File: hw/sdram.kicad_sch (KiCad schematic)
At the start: 25 parts, among them U1 NDS36PT5-16ET, U8 T20Q144xx, X2 ECS-2520MV-250-CM

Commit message: cleanup of trion project
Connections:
- net A11 renamed SDRAM_A11
- net A12 renamed SDRAM_A12
- net CKE renamed SDRAM_CKE
- net ETH0_CLK_OUT: no longer names the net of U8.93 (GPIOR_123_CLK12_CDI20)
- net ETH0_GPIO_1: no longer names the net of U8.89 (GPIOR_129_CTRL10)
- net ETH0_GPIO_2: no longer names the net of U8.90 (GPIOR_128_CTRL11)
- net LED0: no longer names the net of U8.92 (GPIOR_125_CLK10)
- net LED1: no longer names the net of U8.84 (GPIOR_135_CDI17)
- net LED2: no longer names the net of U8.83 (GPIOR_136_CDI16)
- net LED3: no longer names the net of U8.82 (GPIOR_138)
- net LED4: no longer names the net of R22.2, U8.80 (GPIOR_149_CBUS2)
- net LED5: no longer names the net of R23.2, U8.79 (GPIOR_150_CBUS1)
- net LED6: no longer names the net of R24.2, U8.78 (GPIOR_151_CBUS0)
- net LED7: no longer names the net of U8.76 (GPIOR_155)
- no-connect marks 2 -> 13
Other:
- moved on the sheet: R1
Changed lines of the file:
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@@
   (junction (at 67.31 45.72) (diameter 0) (color 0 0 0 0)
   )
+  (junction (at 24.638 101.6) (diameter 0) (color 0 0 0 0)
+  )
   (junction (at 45.72 166.37) (diameter 0) (color 0 0 0 0)
   )
   (junction (at 48.26 40.64) (diameter 0) (color 0 0 0 0)
   )
-  (junction (at 31.75 101.6) (diameter 0) (color 0 0 0 0)
-  )
   (junction (at 38.1 168.91) (diameter 0) (color 0 0 0 0)
   )
@@
   (junction (at 74.93 40.64) (diameter 0) (color 0 0 0 0)
   )
+  (no_connect (at 27.94 171.45))
+  (no_connect (at 160.02 151.13))
+  (no_connect (at 215.9 151.13))
+  (no_connect (at 148.59 97.79))
+  (no_connect (at 116.84 166.37))
+  (no_connect (at 160.02 148.59))
   (no_connect (at 219.71 113.03))
+  (no_connect (at 160.02 146.05))
+  (no_connect (at 215.9 148.59))
+  (no_connect (at 27.94 168.91))
+  (no_connect (at 215.9 146.05))
   (no_connect (at 219.71 110.49))
+  (no_connect (at 27.94 166.37))
   (wire (pts (xy 107.95 168.91) (xy 128.27 168.91))
     (stroke (width 0) (type default))
@@
     (stroke (width 0) (type default))
   )
+  (wire (pts (xy 24.638 101.6) (xy 44.45 101.6))
+    (stroke (width 0) (type default))
+  )
   (wire (pts (xy 57.15 124.46) (xy 57.15 125.73))
     (stroke (width 0) (type default))
@@
     (stroke (width 0) (type default))
   )
-  (wire (pts (xy 31.75 101.6) (xy 44.45 101.6))
-    (stroke (width 0) (type default))
-  )
   (wire (pts (xy 71.12 45.72) (xy 74.93 45.72))
     (stroke (width 0) (type default))
@@
     (stroke (width 0) (type default))
   )
-  (wire (pts (xy 31.75 100.33) (xy 31.75 101.6))
+  (wire (pts (xy 24.638 100.33) (xy 24.638 101.6))
     (stroke (width 0) (type default))
   )
@@
     (stroke (width 0) (type default))
   )
-  (wire (pts (xy 27.94 101.6) (xy 31.75 101.6))
+  (wire (pts (xy 20.828 101.6) (xy 24.638 101.6))
     (stroke (width 0) (type default))
   )
@@
     (effects (font (size 1.27 1.27)) (justify left bottom))
   )
-  (label "CSb" (at 27.94 101.6 180) (fields_autoplaced)
+  (label "CSb" (at 20.828 101.6 180) (fields_autoplaced)
     (effects (font (size 1.27 1.27)) (justify right bottom))
   )
@@
     )
   )
-  (global_label "LED0" (shape output) (at 160.02 146.05 180) (fields_autoplaced)
-    (effects (font (size 1.27 1.27)) (justify right))
-    (property "Intersheetrefs" "${INTERSHEET_REFS}" (at 152.3782 146.05 0)
-      (effects (font (size 1.27 1.27)) (justify right) hide)
-    )
-  )
-  (global_label "LED6" (shape output) (at 27.94 171.45 180) (fields_autoplaced)
-    (effects (font (size 1.27 1.27)) (justify right))
-    (property "Intersheetrefs" "${INTERSHEET_REFS}" (at 20.2982 171.45 0)
-      (effects (font (size 1.27 1.27)) (justify right) hide)
-    )
-  )
   (global_label "ULPI_NXT" (shape input) (at 219.71 123.19 0) (fields_autoplaced)
     (effects (font (size 1.27 1.27)) (justify left))
@@
     )
   )
-  (global_label "ETH0_GPIO_2" (shape bidirectional) (at 160.02 148.59 180) (fields_autoplaced)
-    (effects (font (size 1.27 1.27)) (justify right))
-    (property "Intersheetrefs" "${INTERSHEET_REFS}" (at 143.6469 148.59 0)
-      (effects (font (size 1.27 1.27)) (justify right) hide)
-    )
-  )
-  (global_label "ETH0_CLK_OUT" (shape bidirectional) (at 148.59 97.79 0) (fields_autoplaced)
-    (effects (font (size 1.27 1.27)) (justify left))
-    (property "Intersheetrefs" "${INTERSHEET_REFS}" (at 166.475 97.79 0)
-      (effects (font (size 1.27 1.27)) (justify left) hide)
-    )
-  )
-  (global_label "LED7" (shape output) (at 116.84 166.37 0) (fields_autoplaced)
-    (effects (font (size 1.27 1.27)) (justify left))
-    (property "Intersheetrefs" "${INTERSHEET_REFS}" (at 124.4818 166.37 0)
-      (effects (font (size 1.27 1.27)) (justify left) hide)
-    )
-  )
-  (global_label "LED3" (shape output) (at 215.9 151.13 0) (fields_autoplaced)
-    (effects (font (size 1.27 1.27)) (justify left))
-    (property "Intersheetrefs" "${INTERSHEET_REFS}" (at 223.5418 151.13 0)
-      (effects (font (size 1.27 1.27)) (justify left) hide)
-    )
-  )
-  (global_label "LED5" (shape output) (at 27.94 168.91 180) (fields_autoplaced)
-    (effects (font (size 1.27 1.27)) (justify right))
-    (property "Intersheetrefs" "${INTERSHEET_REFS}" (at 20.2982 168.91 0)
-      (effects (font (size 1.27 1.27)) (justify right) hide)
-    )
-  )
   (global_label "SDRAM_A5" (shape input) (at 44.45 78.74 180) (fields_autoplaced)
     (effects (font (size 1.27 1.27)) (justify right))
@@
     )
   )
-  (global_label "LED2" (shape output) (at 215.9 148.59 0) (fields_autoplaced)
-    (effects (font (size 1.27 1.27)) (justify left))
-    (property "Intersheetrefs" "${INTERSHEET_REFS}" (at 223.5418 148.59 0)
-      (effects (font (size 1.27 1.27)) (justify left) hide)
-    )
-  )
-  (global_label "A12" (shape input) (at 44.45 96.52 180) (fields_autoplaced)
+  (global_label "SDRAM_A12" (shape input) (at 44.45 96.52 180) (fields_autoplaced)
     (effects (font (size 1.27 1.27)) (justify right))
-    (property "Intersheetrefs" "${INTERSHEET_REFS}" (at 37.9572 96.52 0)
+    (property "Intersheetrefs" "${INTERSHEET_REFS}" (at 30.7001 96.52 0)
       (effects (font (size 1.27 1.27)) (justify right) hide)
-    )
-  )
-  (global_label "LED1" (shape output) (at 215.9 146.05 0) (fields_autoplaced)
-    (effects (font (size 1.27 1.27)) (justify left))
-    (property "Intersheetrefs" "${INTERSHEET_REFS}" (at 223.5418 146.05 0)
-      (effects (font (size 1.27 1.27)) (justify left) hide)
     )
   )
@@
     )
   )
-  (global_label "LED4" (shape output) (at 27.94 166.37 180) (fields_autoplaced)
-    (effects (font (size 1.27 1.27)) (justify right))
-    (property "Intersheetrefs" "${INTERSHEET_REFS}" (at 20.2982 166.37 0)
-      (effects (font (size 1.27 1.27)) (justify right) hide)
-    )
-  )
-  (global_label "ETH0_GPIO_1" (shape bidirectional) (at 160.02 151.13 180) (fields_autoplaced)
-    (effects (font (size 1.27 1.27)) (justify right))
-    (property "Intersheetrefs" "${INTERSHEET_REFS}" (at 143.6469 151.13 0)
-      (effects (font (size 1.27 1.27)) (justify right) hide)
-    )
-  )
   (global_label "ULPI_RSTb" (shape output) (at 158.75 123.19 180) (fields_autoplaced)
     (effects (font (size 1.27 1.27)) (justify right))
@@
     )
   )
-  (global_label "CKE" (shape input) (at 44.45 104.14 180) (fields_autoplaced)
+  (global_label "SDRAM_CKE" (shape input) (at 44.45 104.14 180) (fields_autoplaced)
     (effects (font (size 1.27 1.27)) (justify right))
-    (property "Intersheetrefs" "${INTERSHEET_REFS}" (at 37.7758 104.14 0)
+    (property "Intersheetrefs" "${INTERSHEET_REFS}" (at 30.5187 104.14 0)
       (effects (font (size 1.27 1.27)) (justify right) hide)
     )
@@
     )
   )
-  (global_label "A11" (shape input) (at 44.45 93.98 180) (fields_autoplaced)
+  (global_label "SDRAM_A11" (shape input) (at 44.45 93.98 180) (fields_autoplaced)
     (effects (font (size 1.27 1.27)) (justify right))
-    (property "Intersheetrefs" "${INTERSHEET_REFS}" (at 37.9572 93.98 0)
+    (property "Intersheetrefs" "${INTERSHEET_REFS}" (at 30.7001 93.98 0)
       (effects (font (size 1.27 1.27)) (justify right) hide)
     )
@@
     )
   )
-  (symbol (lib_id "Device:R_Small") (at 31.75 97.79 0) (unit 1)
-    (in_bom yes) (on_board yes) (dnp no) (fields_autoplaced)
-    (property "Reference" "R1" (at 33.2486 96.5779 0)
-      (effects (font (size 1.27 1.27)) (justify left))
-    )
-    (property "Value" "10k" (at 33.2486 99.0021 0)
-      (effects (font (size 1.27 1.27)) (justify left))
-    )
-    (property "Footprint" "Resistor_SMD:R_0603_1608Metric" (at 31.75 97.79 0)
-      (effects (font (size 1.27 1.27)) hide)
-    )
-    (property "Datasheet" "~" (at 31.75 97.79 0)
+  (symbol (lib_id "Device:R_Small") (at 24.638 97.79 0) (unit 1)
+    (in_bom yes) (on_board yes) (dnp no) (fields_autoplaced)
+    (property "Reference" "R1" (at 26.1366 96.5779 0)
+      (effects (font (size 1.27 1.27)) (justify left))
+    )
+    (property "Value" "10k" (at 26.1366 99.0021 0)
+      (effects (font (size 1.27 1.27)) (justify left))
+    )
+    (property "Footprint" "Resistor_SMD:R_0603_1608Metric" (at 24.638 97.79 0)
+      (effects (font (size 1.27 1.27)) hide)
+    )
+    (property "Datasheet" "~" (at 24.638 97.79 0)
       (effects (font (size 1.27 1.27)) hide)
     )
@@
     )
   )
-  (symbol (lib_id "power:+3V3") (at 31.75 95.25 0) (unit 1)
-    (in_bom yes) (on_board yes) (dnp no) (fields_autoplaced)
-    (property "Reference" "#PWR037" (at 31.75 99.06 0)
-      (effects (font (size 1.27 1.27)) hide)
-    )
-    (property "Value" "+3V3" (at 31.75 91.1169 0)
-      (effects (font (size 1.27 1.27)))
-    )
-    (property "Footprint" "" (at 31.75 95.25 0)
-      (effects (font (size 1.27 1.27)) hide)
-    )
-    (property "Datasheet" "" (at 31.75 95.25 0)
-      (effects (font (size 1.27 1.27)) hide)
-    )
+  (symbol (lib_id "power:+3V3") (at 24.638 95.25 0) (unit 1)
+    (in_bom yes) (on_board yes) (dnp no) (fields_autoplaced)
+    (property "Reference" "#PWR037" (at 24.638 99.06 0)
+      (effects (font (size 1.27 1.27)) hide)
+    )
+    (property "Value" "+3V3" (at 24.638 91.1169 0)
+      (effects (font (size 1.27 1.27)))
+    )
+    (property "Footprint" "" (at 24.638 95.25 0)
+      (effects (font (size 1.27 1.27)) hide)
+    )
+    (property "Datasheet" "" (at 24.638 95.25 0)
+      (effects (font (size 1.27 1.27)) hide)
+    )

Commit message: reannotated trion project and moved PCB
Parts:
- renumbered C13 to C1038, C10 to C1039, C6 to C1040, C7 to C1041, C8 to C1042, C1 to C1043, C2 to C1044, C4 to C1045, C5 to C1046, C9 to C1047, C57 to C1048, C12 to C1049, C15 to C1050, C64 to C1051, C42 to C1052, C3 to C1053, L1 to L1004, R1 to R1022, R30 to R1023, R24 to R1024, R23 to R1025, R22 to R1026, U8 to U1002, U1 to U1004, X2 to X1001

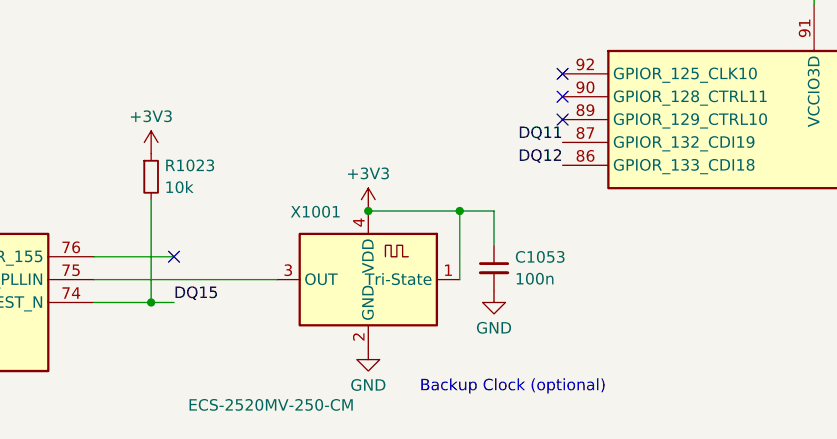
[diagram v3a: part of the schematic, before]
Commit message: moved trion into place; going to 'hide' footprint reference designators...
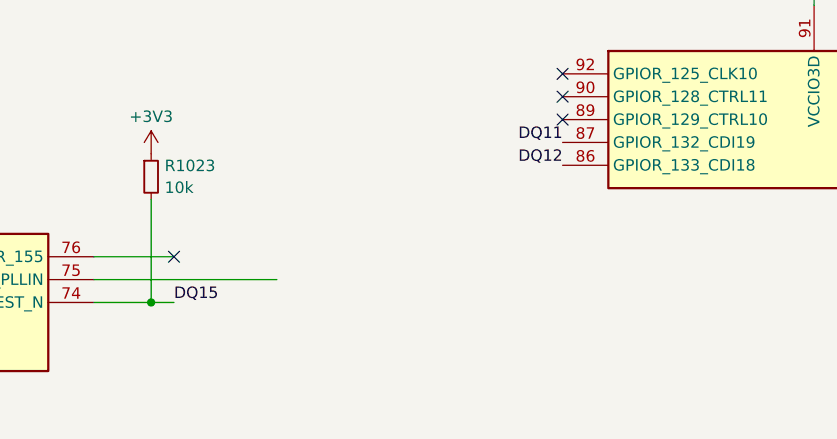
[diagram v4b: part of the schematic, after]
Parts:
- removed C1053: 100n, Capacitor_SMD:C_0603_1608Metric, symbol Device:C_Small
- removed X1001: ECS-2520MV-250-CM, Oscillator:Oscillator_SMD_ECS_2520MV-xxx-xx-4Pin_2.5x2.0mm, symbol Oscillator:ECS-2520MV-xxx-xx
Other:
- note removed: "Backup Clock (optional)"
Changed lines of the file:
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@@
   (junction (at 59.69 40.64) (diameter 0) (color 0 0 0 0)
   )
-  (junction (at 148.59 161.29) (diameter 0) (color 0 0 0 0)
-  )
   (junction (at 74.93 45.72) (diameter 0) (color 0 0 0 0)
   )
@@
   )
   (junction (at 54.61 125.73) (diameter 0) (color 0 0 0 0)
-  )
-  (junction (at 138.43 161.29) (diameter 0) (color 0 0 0 0)
   )
   (junction (at 40.64 40.64) (diameter 0) (color 0 0 0 0)
@@
     (stroke (width 0) (type default))
   )
-  (wire (pts (xy 152.4 165.1) (xy 152.4 161.29))
-    (stroke (width 0) (type default))
-  )
   (wire (pts (xy 54.61 46.99) (xy 52.07 46.99))
     (stroke (width 0) (type default))
@@
     (stroke (width 0) (type default))
   )
-  (wire (pts (xy 152.4 161.29) (xy 148.59 161.29))
-    (stroke (width 0) (type default))
-  )
   (wire (pts (xy 118.11 80.01) (xy 118.11 72.39))
     (stroke (width 0) (type default))
@@
     (stroke (width 0) (type default))
   )
-  (wire (pts (xy 148.59 161.29) (xy 138.43 161.29))
-    (stroke (width 0) (type default))
-  )
   (wire (pts (xy 114.3 171.45) (xy 114.3 160.02))
     (stroke (width 0) (type default))
@@
     (stroke (width 0) (type default))
   )
-  (wire (pts (xy 148.59 168.91) (xy 148.59 161.29))
-    (stroke (width 0) (type default))
-  )
   (wire (pts (xy 67.31 45.72) (xy 71.12 45.72))
     (stroke (width 0) (type default))
@@
   (wire (pts (xy 57.15 53.34) (xy 57.15 46.99))
     (stroke (width 0) (type default))
-  )
-  (text "Backup Clock (optional)" (at 144.145 181.61 0)
-    (effects (font (size 1.27 1.27)) (justify left bottom))
   )
   (text "NOTE:\nSDRAM not used for Ethernet/PTP application.\nCan be loaded to test the SDRAM controller\non the same PCB."
@@
         (path "/8c6e15e3-1804-4f03-8a4f-3cb8420d9169/1b523d49-ff11-41b3-8609-dd0dd8346ed0"
           (reference "#PWR01060") (unit 1)
-        )
-      )
-    )
-  )
-  (symbol (lib_id "power:+3V3") (at 138.43 161.29 0) (mirror y) (unit 1)
-    (in_bom yes) (on_board yes) (dnp no) (fields_autoplaced)
-    (property "Reference" "#PWR01071" (at 138.43 165.1 0)
-      (effects (font (size 1.27 1.27)) hide)
-    )
-    (property "Value" "+3V3" (at 138.43 157.1569 0)
-      (effects (font (size 1.27 1.27)))
-    )
-    (property "Footprint" "" (at 138.43 161.29 0)
-      (effects (font (size 1.27 1.27)) hide)
-    )
-    (property "Datasheet" "" (at 138.43 161.29 0)
-      (effects (font (size 1.27 1.27)) hide)
-    )
-    (pin "1")
-    (instances
-      (project "usbadc"
-        (path "/7c8a1f8d-8834-4c9b-aaae-1f231e9b09a1/d9cd2a48-41b0-4b01-a978-0843576735ad/1b523d49-ff11-41b3-8609-dd0dd8346ed0"
-          (reference "#PWR01071") (unit 1)
-        )
-      )
-      (project "trion-8-test"
-        (path "/8c6e15e3-1804-4f03-8a4f-3cb8420d9169/1b523d49-ff11-41b3-8609-dd0dd8346ed0"
-          (reference "#PWR01071") (unit 1)
         )
       )
@@
     )
   )
-  (symbol (lib_id "Device:C_Small") (at 152.4 167.64 0) (unit 1)
-    (in_bom yes) (on_board yes) (dnp no) (fields_autoplaced)
-    (property "Reference" "C1053" (at 154.7241 166.4342 0)
-      (effects (font (size 1.27 1.27)) (justify left))
-    )
-    (property "Value" "100n" (at 154.7241 168.8584 0)
-      (effects (font (size 1.27 1.27)) (justify left))
-    )
-    (property "Footprint" "Capacitor_SMD:C_0603_1608Metric" (at 152.4 167.64 0)
-      (effects (font (size 1.27 1.27)) hide)
-    )
-    (property "Datasheet" "~" (at 152.4 167.64 0)
-      (effects (font (size 1.27 1.27)) hide)
-    )
-    (property "Manufacturer" "Samsung" (at 152.4 167.64 0)
-      (effects (font (size 1.27 1.27)) hide)
-    )
-    (property "Part" "CL10B104KB8NFN" (at 152.4 167.64 0)
-      (effects (font (size 1.27 1.27)) hide)
-    )
-    (pin "1")
-    (pin "2")
-    (instances
-      (project "usbadc"
-        (path "/7c8a1f8d-8834-4c9b-aaae-1f231e9b09a1/d9cd2a48-41b0-4b01-a978-0843576735ad/1b523d49-ff11-41b3-8609-dd0dd8346ed0"
-          (reference "C1053") (unit 1)
-        )
-      )
-      (project "trion-8-test"
-        (path "/8c6e15e3-1804-4f03-8a4f-3cb8420d9169/1b523d49-ff11-41b3-8609-dd0dd8346ed0"
-          (reference "C1053") (unit 1)
-        )
-      )
-    )
-  )
   (symbol (lib_id "FPGA_Efinix_Trion:T8Q144xx") (at 189.23 118.11 0) (unit 4)
     (in_bom yes) (on_board yes) (dnp no)
@@
     )
   )
-  (symbol (lib_id "power:GND") (at 152.4 170.18 0) (unit 1)
-    (in_bom yes) (on_board yes) (dnp no) (fields_autoplaced)
-    (property "Reference" "#PWR01072" (at 152.4 176.53 0)
-      (effects (font (size 1.27 1.27)) hide)
-    )
-    (property "Value" "GND" (at 152.4 174.3131 0)
-      (effects (font (size 1.27 1.27)))
-    )
-    (property "Footprint" "" (at 152.4 170.18 0)
-      (effects (font (size 1.27 1.27)) hide)
-    )
-    (property "Datasheet" "" (at 152.4 170.18 0)
-      (effects (font (size 1.27 1.27)) hide)
-    )
-    (pin "1")
-    (instances
-      (project "usbadc"
-        (path "/7c8a1f8d-8834-4c9b-aaae-1f231e9b09a1/d9cd2a48-41b0-4b01-a978-0843576735ad/1b523d49-ff11-41b3-8609-dd0dd8346ed0"
-          (reference "#PWR01072") (unit 1)
-        )
-      )
-      (project "trion-8-test"
-        (path "/8c6e15e3-1804-4f03-8a4f-3cb8420d9169/1b523d49-ff11-41b3-8609-dd0dd8346ed0"
-          (reference "#PWR01072") (unit 1)
-        )
-      )
-    )
-  )
   (symbol (lib_id "FPGA_Efinix_Trion:T8Q144xx") (at 187.96 54.61 0) (unit 2)
     (in_bom yes) (on_board yes) (dnp no) (fields_autoplaced)
@@
     )
   )
-  (symbol (lib_id "Oscillator:ECS-2520MV-xxx-xx") (at 138.43 168.91 0) (mirror y) (unit 1)
-    (in_bom yes) (on_board yes) (dnp no)
-    (property "Reference" "X1001" (at 132.588 161.417 0)
-      (effects (font (size 1.27 1.27)))
-    )
-    (property "Value" "ECS-2520MV-250-CM" (at 127.635 182.88 0)
-      (effects (font (size 1.27 1.27)))
-    )
-    (property "Footprint" "Oscillator:Oscillator_SMD_ECS_2520MV-xxx-xx-4Pin_2.5x2.0mm" (at 127 177.8 0)
-      (effects (font (size 1.27 1.27)) hide)
-    )
-    (property "Datasheet" "https://www.ecsxtal.com/store/pdf/ECS-2520MV.pdf" (at 142.875 165.735 0)
-      (effects (font (size 1.27 1.27)) hide)
-    )
-    (property "Manufacturer" "ECS" (at 138.43 168.91 0)
-      (effects (font (size 1.27 1.27)) hide)
-    )
-    (property "Part" "ECS-2520MV-250-CL-TR" (at 138.43 168.91 0)
-      (effects (font (size 1.27 1.27)) hide)
-    )
-    (pin "1")
-    (pin "2")
-    (pin "4")
-    (pin "3")
-    (instances
-      (project "usbadc"
-        (path "/7c8a1f8d-8834-4c9b-aaae-1f231e9b09a1/d9cd2a48-41b0-4b01-a978-0843576735ad/1b523d49-ff11-41b3-8609-dd0dd8346ed0"
-          (reference "X1001") (unit 1)
-        )
-      )
-      (project "trion-8-test"
-        (path "/8c6e15e3-1804-4f03-8a4f-3cb8420d9169/1b523d49-ff11-41b3-8609-dd0dd8346ed0"
-          (reference "X1001") (unit 1)
-        )
-      )
-    )
-  )
   (symbol (lib_id "power:+3V3") (at 62.23 151.13 0) (unit 1)
     (in_bom yes) (on_board yes) (dnp no) (fields_autoplaced)
@@
         )
       )
-    )
-  )
-  (symbol (lib_id "power:GND") (at 138.43 176.53 0) (unit 1)
-    (in_bom yes) (on_board yes) (dnp no) (fields_autoplaced)
-    (property "Reference" "#PWR01073" (at 138.43 182.88 0)
-      (effects (font (size 1.27 1.27)) hide)
-    )
-    (property "Value" "GND" (at 138.43 180.6631 0)
-      (effects (font (size 1.27 1.27)))
-    )
-    (property "Footprint" "" (at 138.43 176.53 0)
-      (effects (font (size 1.27 1.27)) hide)
-    )
-    (property "Datasheet" "" (at 138.43 176.53 0)
-      (effects (font (size 1.27 1.27)) hide)
-    )
-    (pin "1")
-    (instances
-      (project "usbadc"
-        (path "/7c8a1f8d-8834-4c9b-aaae-1f231e9b09a1/d9cd2a48-41b0-4b01-a978-0843576735ad/1b523d49-ff11-41b3-8609-dd0dd8346ed0"
-          (reference "#PWR01073") (unit 1)
-        )
-      )
-      (project "trion-8-test"
-        (path "/8c6e15e3-1804-4f03-8a4f-3cb8420d9169/1b523d49-ff11-41b3-8609-dd0dd8346ed0"
-          (reference "#PWR01073") (unit 1)
-        )
-      )
